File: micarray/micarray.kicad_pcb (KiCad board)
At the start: 4 copper layers, 84 x 84 mm, 37 parts, among them IC1 74LCX125MTCX, J1 Previous, J2 Next, J3 MCHStreamer J3

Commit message: save
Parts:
- J1: footprint Connector_PinSocket_2.54mm:PinSocket_1x09_P2.54mm_Horizontal -> Connector_PinSocket_2.54mm:PinSocket_2x05_P2.54mm_Horizontal
- J2: footprint Connector_PinHeader_2.54mm:PinHeader_1x09_P2.54mm_Horizontal -> Connector_PinHeader_2.54mm:PinHeader_2x05_P2.54mm_Horizontal
- moved R14 16.2 mm to (90.2, 61.6)
- moved J3 16.1 mm to (91.6, 76.9)
- moved R11 11.8 mm to (106.0, 57.0), turned to 45 degrees
- moved J2 11.0 mm to (141.5, 28.0)
- moved J1 10.4 mm to (78.0, 91.5)
- moved R9 10.0 mm to (101.9, 53.1), turned to 45 degrees
- moved IC1 8.56 mm to (103.9, 55.1), turned to 45 degrees
- moved R10 8.04 mm to (101.2, 60.3), turned to 0 degrees
- moved L5 5.90 mm to (104.3, 50.7), turned to 45 degrees
- moved L4 5.83 mm to (133.2, 35.3), turned to 90 degrees
- moved C9 5.80 mm to (101.9, 50.7), turned to 45 degrees
- moved C10 4.77 mm to (100.8, 49.7), turned to 45 degrees
- moved R13 4.30 mm to (108.3, 50.1), turned to 90 degrees
- moved R7 3.80 mm to (138.1, 35.2)
- moved C8 3.77 mm to (134.7, 35.4), turned to -90 degrees
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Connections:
- J1 pad 1: PDM_DATA7 -> PDM_DATA2
- J1 pad 2: PDM_DATA6 -> PDM_DATA3
- J1 pad 3: PDM_DATA5 -> PDM_DATA4
- J1 pad 4: PDM_DATA4 -> PDM_DATA5
- J1 pad 5: PDM_DATA3 -> PDM_DATA6
- J1 pad 6: PDM_DATA2 -> PDM_DATA7
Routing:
- net PDM_DATA4: track 139.7 -> 0.00 mm
- net PDM_DATA5: track 138.0 -> 0.00 mm
- net PDM_DATA2: track 137.5 -> 0.00 mm
- net PDM_DATA3: track 134.7 -> 0.00 mm
- net PDM_DATA0: track 135.7 -> 28.9 mm
- net PDM_DATA1: track 123.4 -> 74.5 mm
- net +3V3: track 30.9 -> 0.00 mm, vias 3 -> 0
- net PDM_CLK-IN: track 116.4 -> 100.3 mm
- net PDM_DATA7: track 15.6 -> 0.00 mm
- net PDM_DATA6: track 9.49 -> 0.00 mm
- net PDM_CLK1: track 6.98 -> 1.49 mm, vias 2 -> 0
- net PDM_CLK2: track 16.2 -> 12.1 mm
- net PDM_CLK3: track 42.9 -> 38.8 mm
- net Net-(J3-Pin_12): track 2.65 -> 0.00 mm
- net Net-(IC1-O0): track 6.25 -> 4.50 mm
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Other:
- board size 84 x 84 mm -> 75 x 75 mm

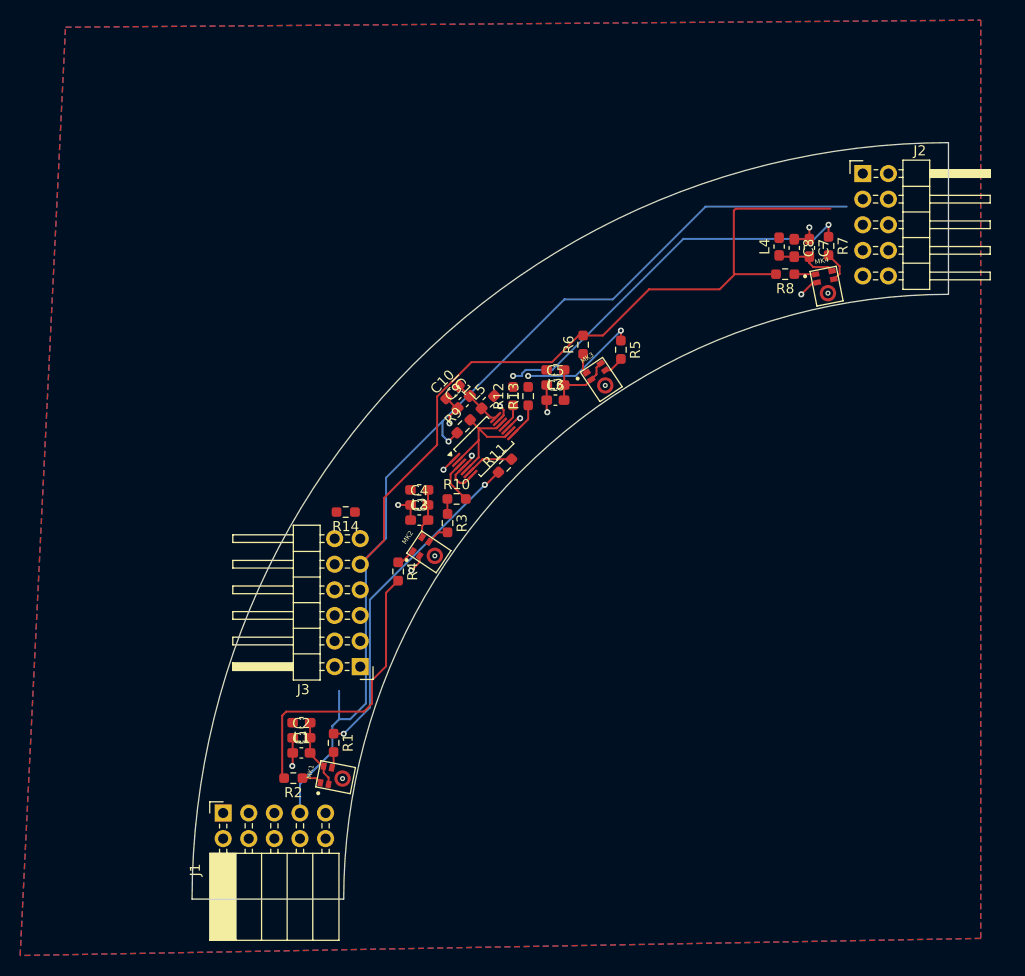
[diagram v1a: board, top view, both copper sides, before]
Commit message: All traces, no ground to mic
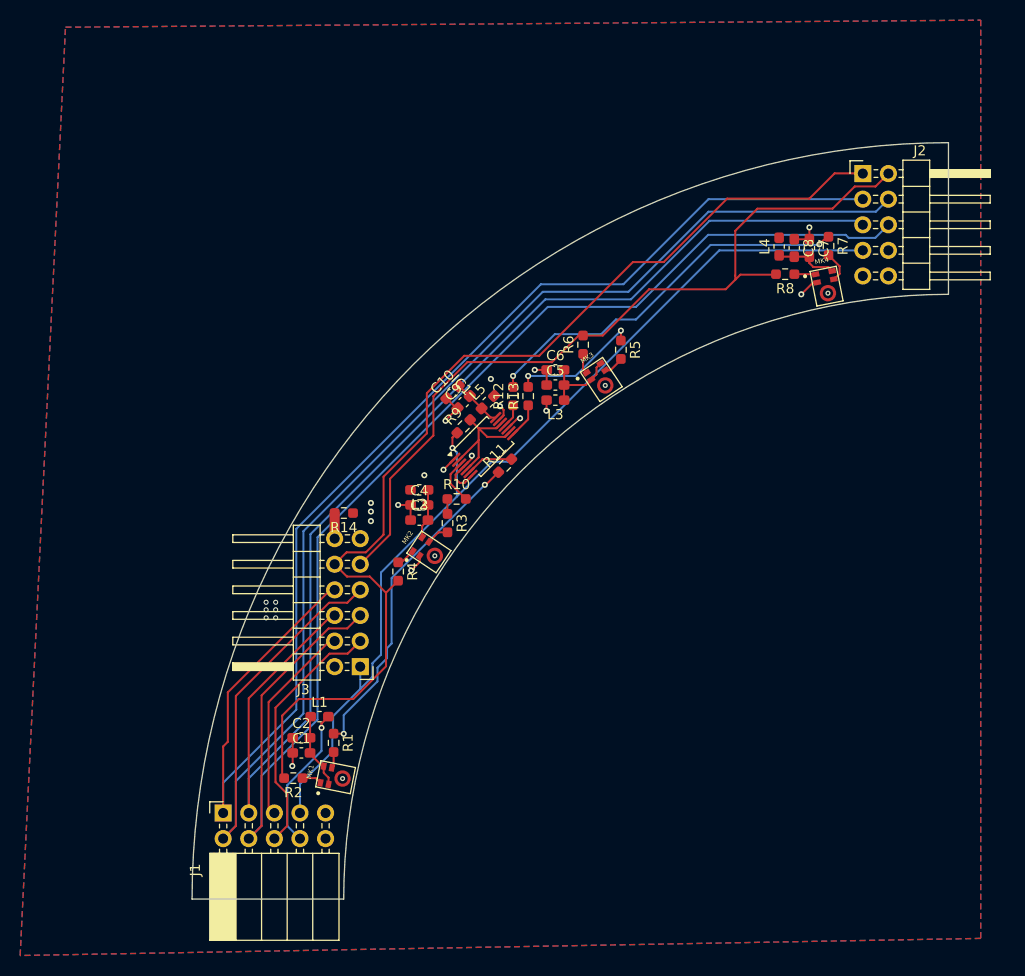
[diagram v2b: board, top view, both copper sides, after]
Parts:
- moved C6 3.00 mm to (111.0, 47.5)
- moved L3 3.00 mm to (111.0, 50.5)
- moved L1 1.90 mm to (87.6, 81.9), turned to 0 degrees
- moved R14 0.21 mm to (90.0, 61.7)
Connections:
- J2 pad 1: PDM_DATA5 -> PDM_DATA0
- J2 pad 2: PDM_DATA4 -> PDM_DATA1
- J2 pad 3: PDM_DATA3 -> PDM_DATA2
- J2 pad 4: PDM_DATA2 -> PDM_DATA3
- J2 pad 5: PDM_DATA1 -> PDM_DATA4
- J2 pad 6: PDM_DATA0 -> PDM_DATA5
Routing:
- net PDM_DATA3: track 0.00 -> 136.9 mm
- net PDM_DATA5: track 0.00 -> 130.3 mm
- net PDM_DATA2: track 0.00 -> 127.9 mm
- net PDM_DATA4: track 0.00 -> 121.4 mm
- net PDM_DATA0: track 28.9 -> 108.0 mm
- net PDM_DATA7: track 0.00 -> 25.1 mm
- net PDM_DATA6: track 0.00 -> 20.3 mm
- net +3V3: track 0.00 -> 15.4 mm, vias 0 -> 13
- net PDM_DATA1: track 74.5 -> 81.1 mm
- net PDM_CLK-IN: track 100.3 -> 96.9 mm
- net Net-(J3-Pin_12): track 0.00 -> 2.54 mm
- net PDM_CLK2: track 12.1 -> 13.1 mm
- net Net-(MK1-SELECT): track 6.82 -> 7.61 mm
- net PDM_CLK3: track 38.8 -> 38.1 mm

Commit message: Mic GND connection, silkscreen cleanup
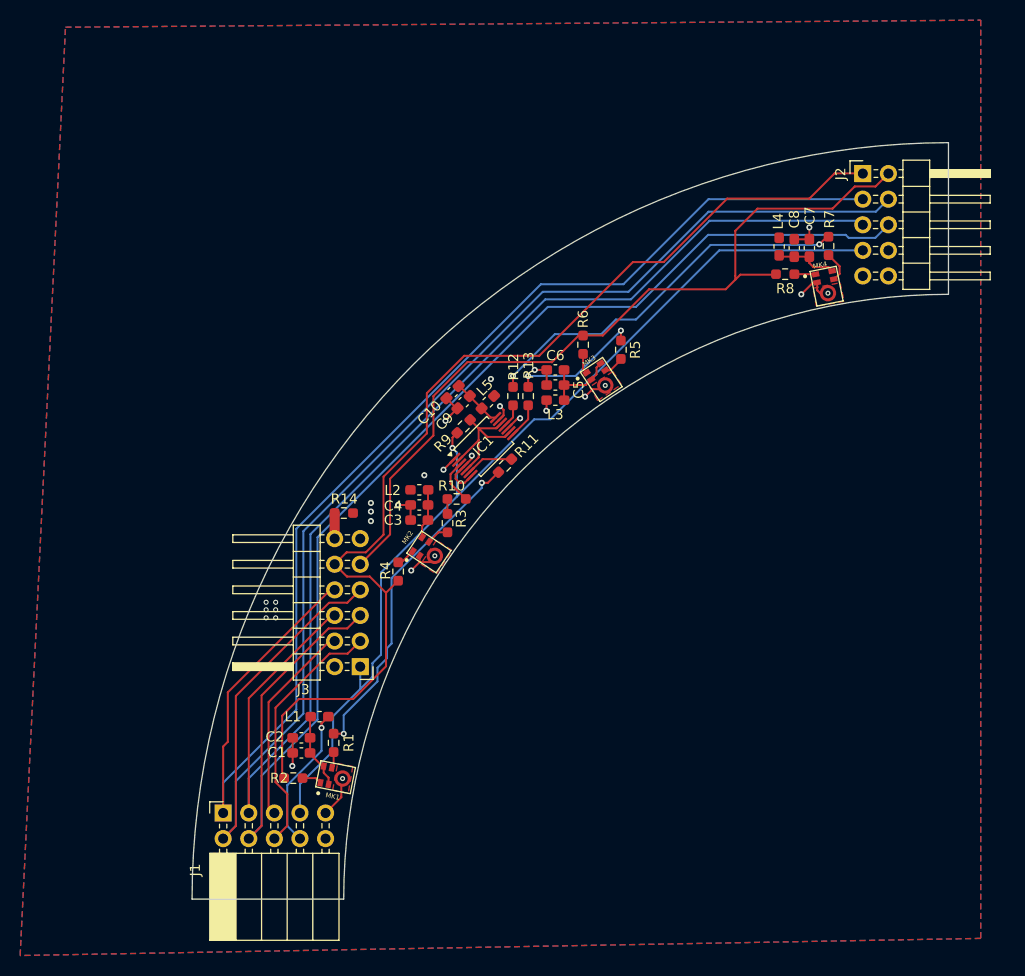
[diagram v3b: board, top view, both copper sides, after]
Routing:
- net GND: track 28.1 -> 35.9 mm, vias 11 -> 12
- added copper zone on F.Cu, net GND

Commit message: JLC IDs added, pre TSSOP14
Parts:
- removed R14: 0, Resistor_SMD:R_0603_1608Metric_Pad0.98x0.95mm_HandSolder
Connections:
- J3 pad 12: Net-(J3-Pin_12) -> +3V3
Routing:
- net Net-(J3-Pin_12): track 2.54 -> 0.00 mm

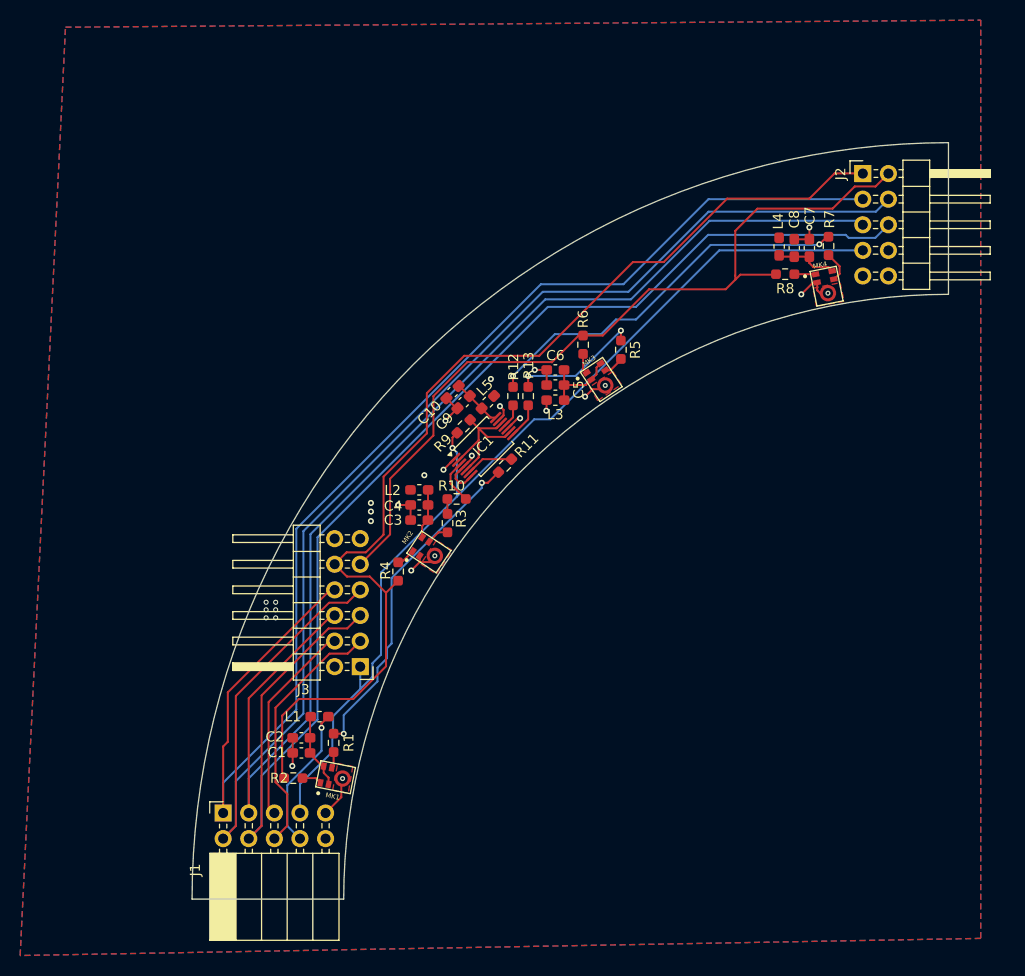
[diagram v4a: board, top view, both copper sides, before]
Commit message: Change Mic and IC footprint
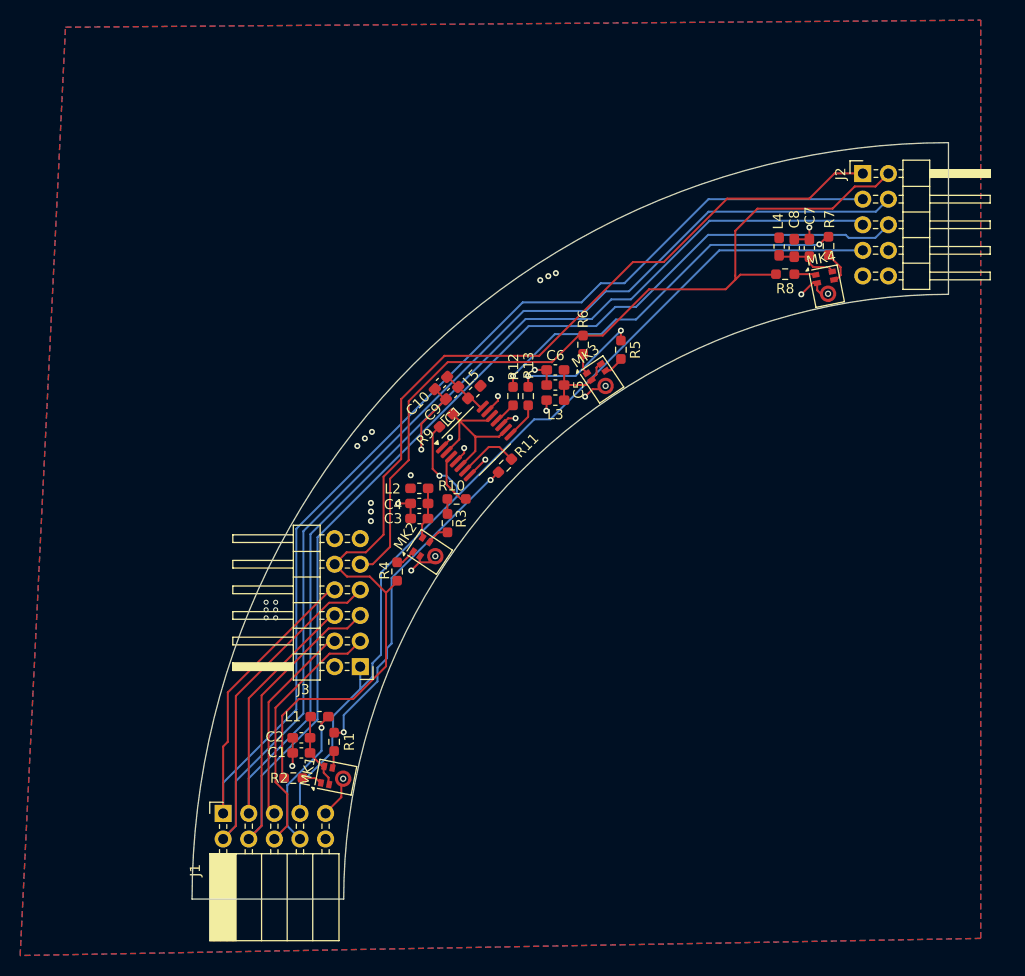
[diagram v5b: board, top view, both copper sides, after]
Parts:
- IC1: footprint Package_SO:TSSOP-14_4.4x3.6mm_P0.4mm -> Package_SO:TSSOP-14_4.4x5mm_P0.65mm
- MK1, MK2, MK3, MK4: footprint SPH1668LM4H_1:MIC_SPH1668LM4H-1 -> Sensor_Audio:Knowles_LGA-5_3.5x2.65mm
- moved R9 1.85 mm to (100.2, 52.5)
- moved L5 1.68 mm to (103.0, 49.7)
- moved C9 1.46 mm to (100.8, 49.8)
- moved C10 1.46 mm to (99.7, 48.8)
- moved IC1 0.93 mm to (103.2, 54.5)
- moved C3 0.15 mm to (97.5, 62.2)
- moved C4 0.15 mm to (97.5, 60.8)
- moved L2 0.15 mm to (97.5, 59.2)
- moved R1 0.11 mm to (89.0, 84.4)
- moved R4 0.10 mm to (95.3, 67.5)
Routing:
- net GND: track 35.9 -> 39.7 mm, vias 12 -> 13
- net Net-(IC1-A0): track 14.9 -> 17.1 mm
- net PDM_CLK-IN: track 96.9 -> 98.8 mm
- net PDM_DATA1: track 81.1 -> 83.0 mm
- net Net-(IC1-O1): track 4.76 -> 6.07 mm
- net PDM_DATA0: track 108.0 -> 109.1 mm
- net Net-(IC1-O0): track 4.50 -> 5.45 mm
- net +3V3: vias 13 -> 19
- removed copper zone on F.Cu, net GND
